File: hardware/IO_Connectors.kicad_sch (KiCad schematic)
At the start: 31 parts, among them J29 RJ12_Shielded, J3 USB_B_Micro, U8 TJA1040

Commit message: Convert SCH files to latest version. Fix DRC Warnings in PrntrBoard.
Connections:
- net ~EXP_CS renamed ~{EXP_CS}
- net ~EXP_CS2 renamed ~{EXP_CS2}
- net ~LCD_E renamed ~{LCD_E}
- net ~RESET renamed ~{RESET}
- net ~SD_CS renamed ~{SD_CS}
- net ~SD_DETECT renamed ~{SD_DETECT}
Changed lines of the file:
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@@
-(kicad_sch (version 20210126) (generator eeschema)
+(kicad_sch (version 20210621) (generator eeschema)
   (paper "A4")
   (junction (at 69.215 106.68) (diameter 1.016) (color 0 0 0 0))
@@
     (effects (font (size 1.27 1.27)) (justify right bottom))
   )
-  (global_label "~EXP_CS" (shape input) (at 32.385 123.19 180)
+  (global_label "~{EXP_CS}" (shape input) (at 32.385 123.19 180)
     (effects (font (size 1.27 1.27)) (justify right))
     (property "Intersheet References" "${INTERSHEET_REFS}" (id 0) (at 0 0 0)
@@
     )
   )
-  (global_label "~RESET" (shape input) (at 38.735 127.635 180)
+  (global_label "~{RESET}" (shape input) (at 38.735 127.635 180)
     (effects (font (size 1.27 1.27)) (justify right))
     (property "Intersheet References" "${INTERSHEET_REFS}" (id 0) (at 0 0 0)
@@
     )
   )
-  (global_label "~LCD_E" (shape input) (at 76.835 113.665 0)
+  (global_label "~{LCD_E}" (shape input) (at 76.835 113.665 0)
     (effects (font (size 1.27 1.27)) (justify left))
     (property "Intersheet References" "${INTERSHEET_REFS}" (id 0) (at 0 0 0)
@@
     )
   )
-  (global_label "~EXP_CS2" (shape input) (at 113.665 67.31 0)
+  (global_label "~{EXP_CS2}" (shape input) (at 113.665 67.31 0)
     (effects (font (size 1.27 1.27)) (justify left))
     (property "Intersheet References" "${INTERSHEET_REFS}" (id 0) (at 125.8873 67.2306 0)
@@
     )
   )
-  (global_label "~EXP_CS" (shape input) (at 113.665 70.485 0)
+  (global_label "~{EXP_CS}" (shape input) (at 113.665 70.485 0)
     (effects (font (size 1.27 1.27)) (justify left))
     (property "Intersheet References" "${INTERSHEET_REFS}" (id 0) (at 0 0 0)
@@
     )
   )
-  (global_label "~SD_CS" (shape input) (at 188.595 72.39 180)
+  (global_label "~{SD_CS}" (shape input) (at 188.595 72.39 180)
     (effects (font (size 1.27 1.27)) (justify right))
     (property "Intersheet References" "${INTERSHEET_REFS}" (id 0) (at 178.7312 72.3106 0)
@@
     )
   )
-  (global_label "~SD_DETECT" (shape input) (at 189.865 75.565 180)
+  (global_label "~{SD_DETECT}" (shape input) (at 189.865 75.565 180)
     (effects (font (size 1.27 1.27)) (justify right))
     (property "Intersheet References" "${INTERSHEET_REFS}" (id 0) (at 24.13 -2.54 0)
@@
     (pin "2")
   )
+  (symbol (lib_id "Jumper:Jumper_2_Open") (at 39.37 123.19 0) (unit 1)
+    (in_bom yes) (on_board yes)
+    (property "Reference" "JP1" (id 0) (at 39.37 117.221 0))
+    (property "Value" "Jumper_2_Open" (id 1) (at 39.37 119.5324 0))
+    (property "Footprint" "Connector_PinHeader_2.54mm:PinHeader_1x02_P2.54mm_Vertical" (id 2) (at 39.37 123.19 0)
+      (effects (font (size 1.27 1.27)) hide)
+    )
+    (property "Datasheet" "~" (id 3) (at 39.37 123.19 0)
+      (effects (font (size 1.27 1.27)) hide)
+    )
+    (property "Part #" "" (id 4) (at 39.37 123.19 0)
+      (effects (font (size 1.27 1.27)) hide)
+    )
+    (property "LCSC Part #" "C160332" (id 5) (at 39.37 123.19 0)
+      (effects (font (size 1.27 1.27)) hide)
+    )
+    (pin "1")
+    (pin "2")
+  )
   (symbol (lib_id "Device:Polyfuse") (at 201.295 115.57 270) (unit 1)
     (in_bom yes) (on_board yes)
@@
       (effects (font (size 1.27 1.27)) hide)
     )
-    (pin "1")
-    (pin "2")
-  )
-  (symbol (lib_id "Jumper:Jumper_2_Open") (at 39.37 123.19 0) (unit 1)
-    (in_bom yes) (on_board yes)
-    (property "Reference" "JP1" (id 0) (at 39.37 117.221 0))
-    (property "Value" "Jumper_2_Open" (id 1) (at 39.37 119.5324 0))
-    (property "Footprint" "Connector_PinHeader_2.54mm:PinHeader_1x02_P2.54mm_Vertical" (id 2) (at 39.37 123.19 0)
-      (effects (font (size 1.27 1.27)) hide)
-    )
-    (property "Datasheet" "~" (id 3) (at 39.37 123.19 0)
-      (effects (font (size 1.27 1.27)) hide)
-    )
-    (property "Part #" "" (id 4) (at 39.37 123.19 0)
-      (effects (font (size 1.27 1.27)) hide)
-    )
-    (property "LCSC Part #" "C160332" (id 5) (at 39.37 123.19 0)
-      (effects (font (size 1.27 1.27)) hide)
-    )

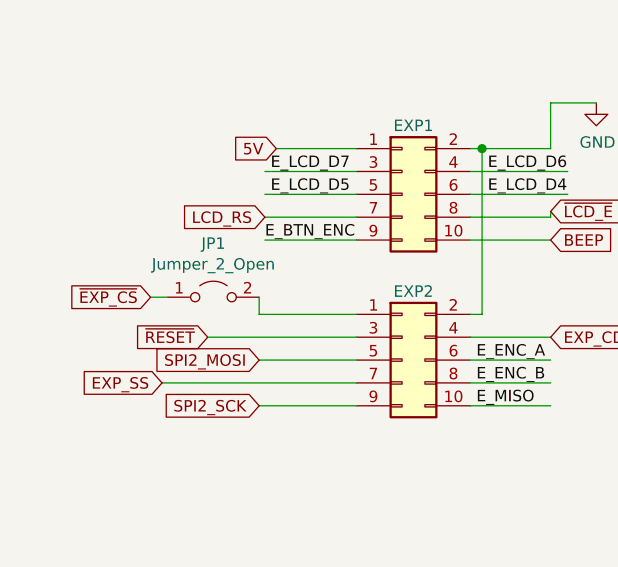
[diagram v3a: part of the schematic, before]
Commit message: Add voltage selection for each stepper driver.
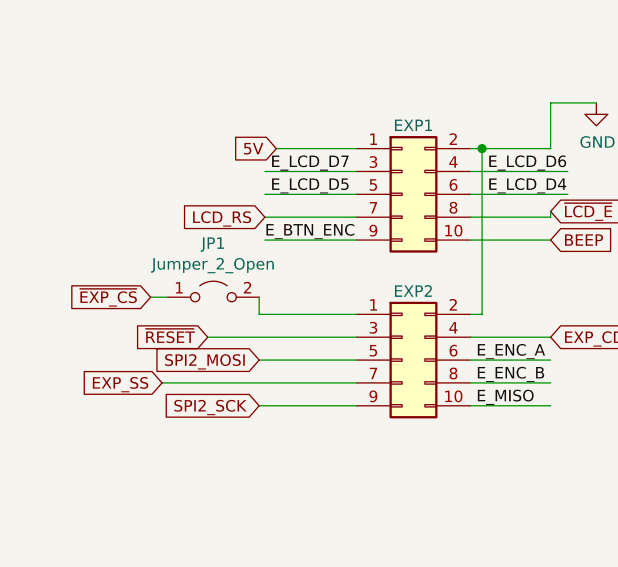
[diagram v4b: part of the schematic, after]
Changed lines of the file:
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@@
+    (pin "2")
+  )
+  (symbol (lib_id "Jumper:Jumper_2_Open") (at 39.37 123.19 0) (unit 1)
+    (in_bom yes) (on_board yes)
+    (property "Reference" "JP1" (id 0) (at 39.37 117.221 0))
+    (property "Value" "Jumper_2_Open" (id 1) (at 39.37 119.5324 0))
+    (property "Footprint" "Connector_PinHeader_2.54mm:PinHeader_1x02_P2.54mm_Vertical" (id 2) (at 39.37 123.19 0)
+      (effects (font (size 1.27 1.27)) hide)
+    )
+    (property "Datasheet" "~" (id 3) (at 39.37 123.19 0)
+      (effects (font (size 1.27 1.27)) hide)
+    )
+    (property "Part #" "" (id 4) (at 39.37 123.19 0)
+      (effects (font (size 1.27 1.27)) hide)
+    )
+    (property "LCSC Part #" "C160332" (id 5) (at 39.37 123.19 0)
+      (effects (font (size 1.27 1.27)) hide)
+    )
+    (pin "1")
     (pin "2")
   )
@@
       (effects (font (size 1.27 1.27)) hide)
     )
-    (pin "1")
-    (pin "2")
-  )
-  (symbol (lib_id "Jumper:Jumper_2_Open") (at 39.37 123.19 0) (unit 1)
-    (in_bom yes) (on_board yes)
-    (property "Reference" "JP1" (id 0) (at 39.37 117.221 0))
-    (property "Value" "Jumper_2_Open" (id 1) (at 39.37 119.5324 0))
-    (property "Footprint" "Connector_PinHeader_2.54mm:PinHeader_1x02_P2.54mm_Vertical" (id 2) (at 39.37 123.19 0)
-      (effects (font (size 1.27 1.27)) hide)
-    )
-    (property "Datasheet" "~" (id 3) (at 39.37 123.19 0)
-      (effects (font (size 1.27 1.27)) hide)
-    )
-    (property "Part #" "" (id 4) (at 39.37 123.19 0)
-      (effects (font (size 1.27 1.27)) hide)
-    )
-    (property "LCSC Part #" "C160332" (id 5) (at 39.37 123.19 0)
-      (effects (font (size 1.27 1.27)) hide)
-    )
